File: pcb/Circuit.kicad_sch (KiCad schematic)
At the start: 46 parts, among them J1 DTM13-12PA-R008, J2 TSW-101-07-T-D, J3 TSW-101-07-T-D, U1 MCP1700-1802E_TO92, U2 CDP68HC68S1, U3 LM2672N-5.0, U4 Teensy4.0, U5 MCP2562-H-P

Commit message: CDP 3d model
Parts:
- removed D3: SD15_SOD323, Diode_THT:D_A-405_P7.62mm_Horizontal, symbol Diode:SD15_SOD323
- added D3: P6KE39CA, Diode_THT:D_DO-15_P10.16mm_Horizontal, symbol Diode_TVS_AKL:P6KE39CA
- C10: footprint Capacitor_THT:C_Radial_D5.0mm_H11.0mm_P2.00mm -> Capacitor_THT:C_Radial_D6.3mm_H7.0mm_P2.50mm
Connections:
- net +12V: now also D3.2 (A)
- net GND: now also D3.1 (K)

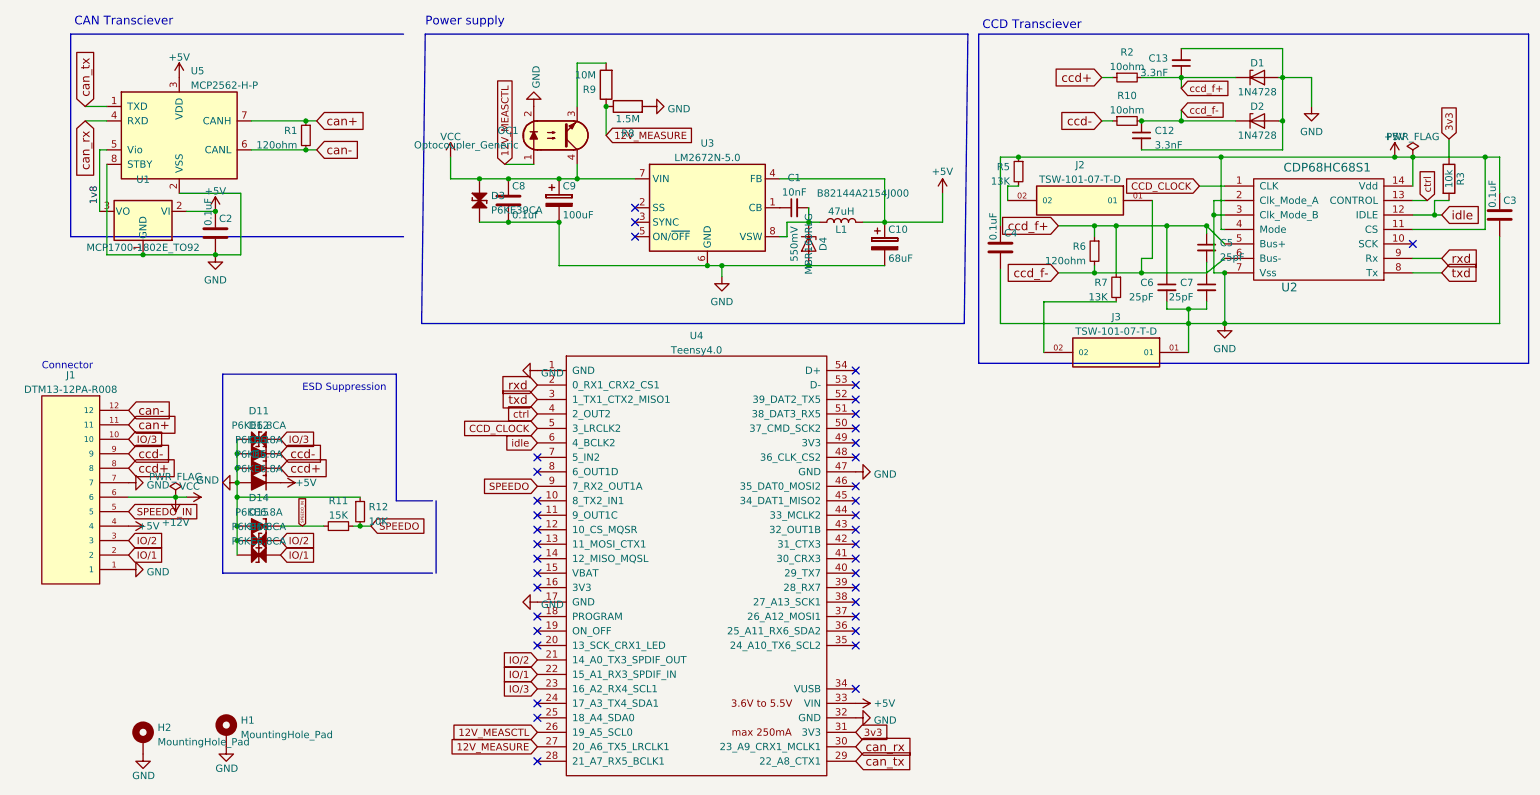
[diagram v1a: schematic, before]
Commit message: Add overvoltage protection to the 12v measure pin
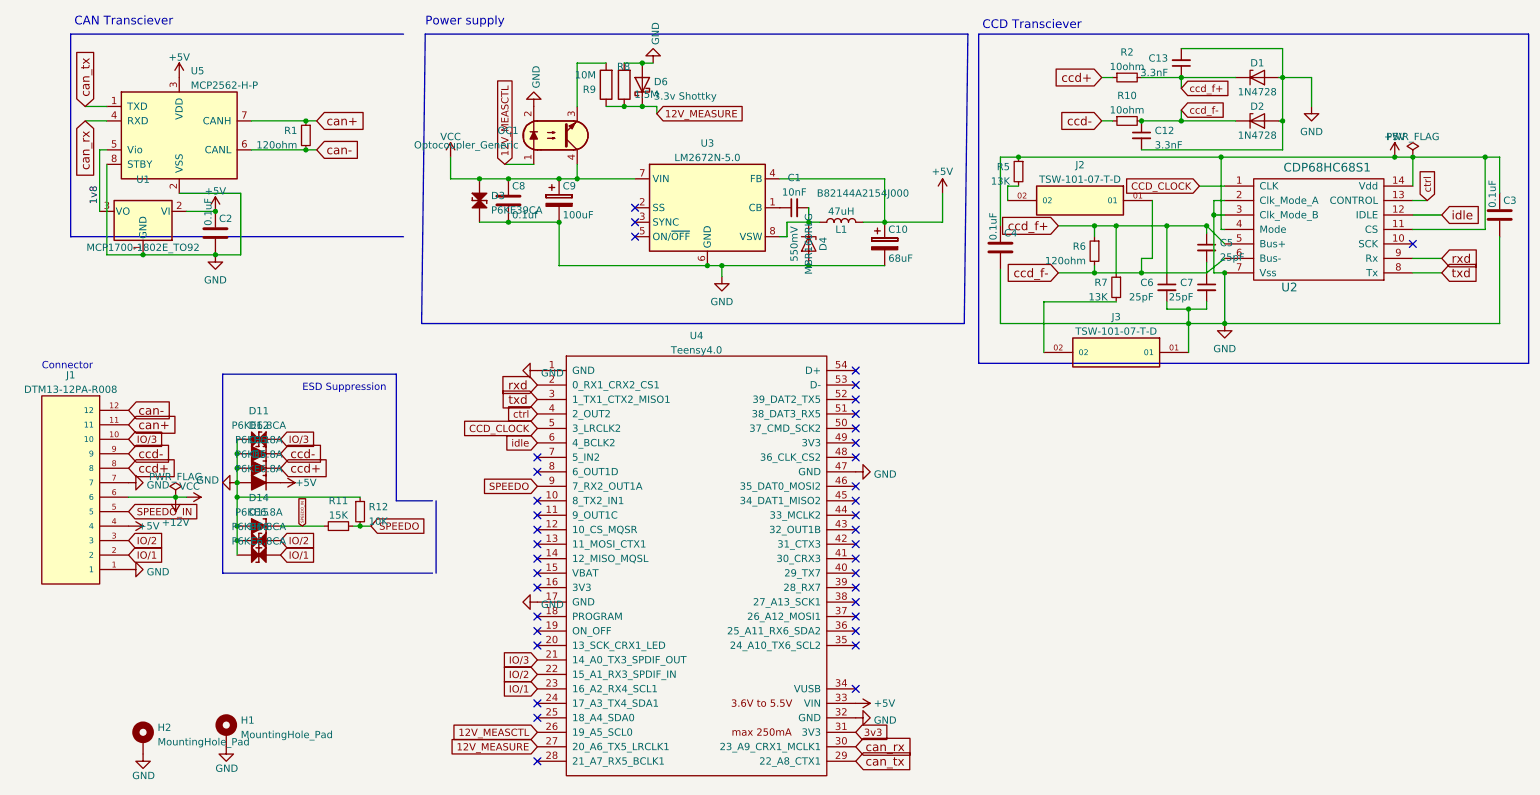
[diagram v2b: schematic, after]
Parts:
- removed R3: 10k, Resistor_THT:R_Axial_DIN0204_L3.6mm_D1.6mm_P5.08mm_Horizontal, symbol ccd_can_bridge-rescue:R
- added D6: 3.3v Shottky, Diode_THT:D_DO-34_SOD68_P7.62mm_Horizontal, symbol Device:D_Schottky
- C9: footprint Capacitor_THT:CP_Radial_D5.0mm_P2.50mm -> Capacitor_THT:CP_Radial_D8.0mm_P3.50mm
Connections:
- net 12V_MEASURE: now also D6.1 (K)
- net GND: now also D6.2 (A)
- net IO/1: now also U4.23 (16_A2_RX4_SCL1); no longer U4.22 (15_A1_RX3_SPDIF_IN)
- net IO/2: now also U4.22 (15_A1_RX3_SPDIF_IN); no longer U4.21 (14_A0_TX3_SPDIF_OUT)
- net IO/3: now also U4.21 (14_A0_TX3_SPDIF_OUT); no longer U4.23 (16_A2_RX4_SCL1)
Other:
- moved on the sheet: R8

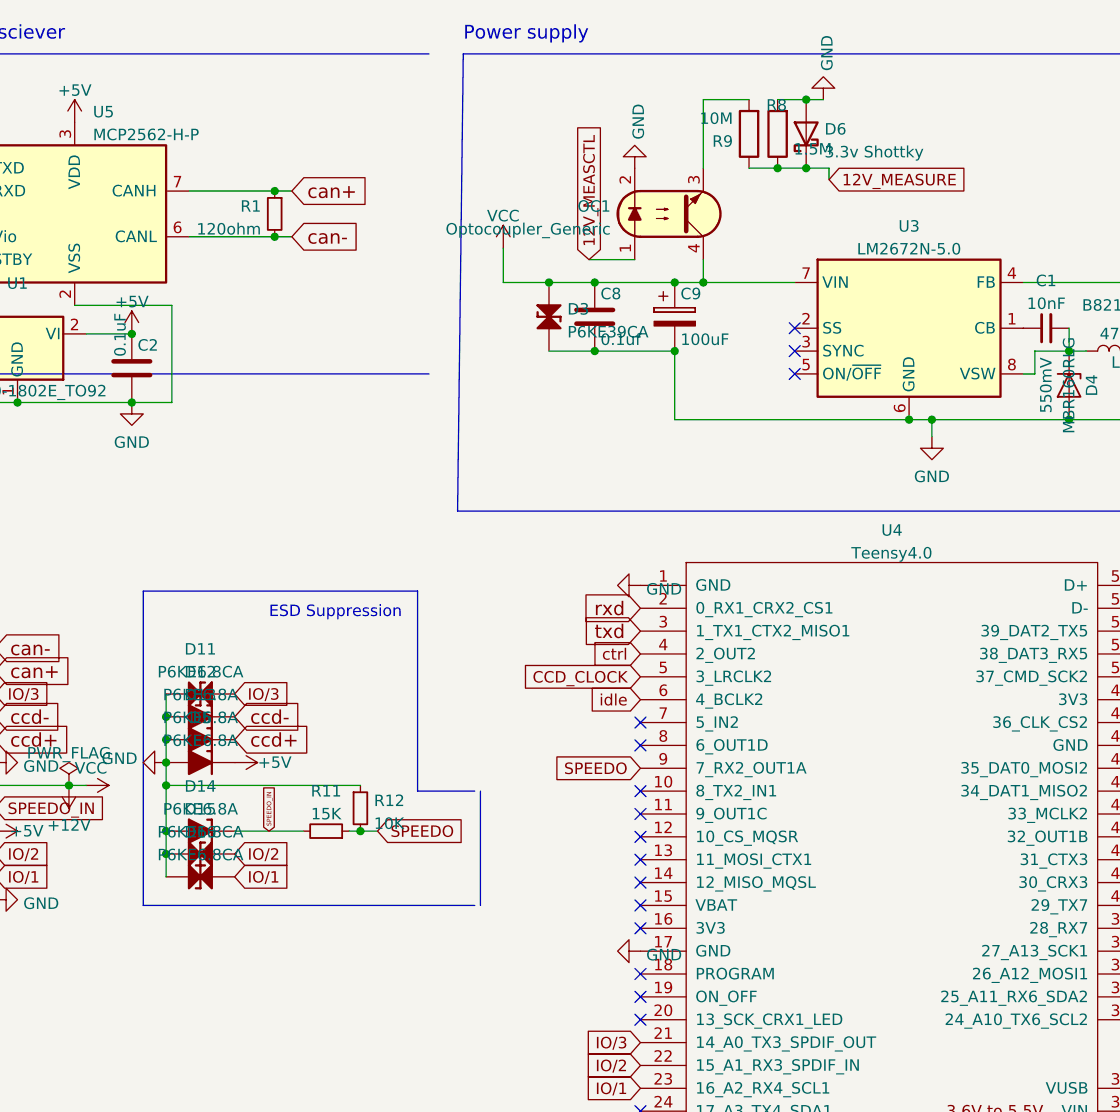
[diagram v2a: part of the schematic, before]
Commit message: Add 3.3v overvolt protection zeners
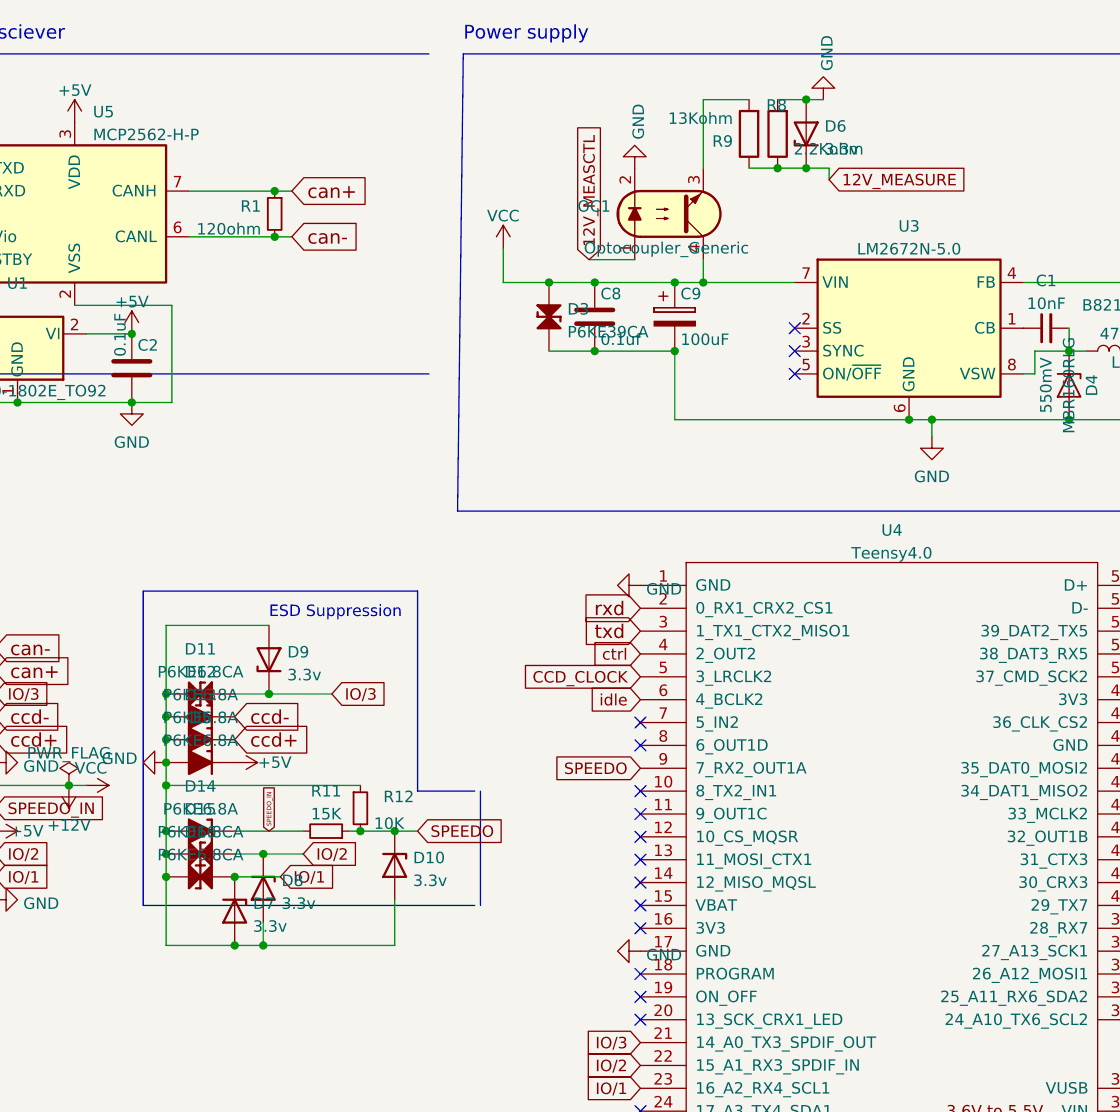
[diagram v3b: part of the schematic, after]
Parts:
- removed D6: 3.3v Shottky, Diode_THT:D_DO-34_SOD68_P7.62mm_Horizontal, symbol Device:D_Schottky
- added D10, D6, D7, D8, D9: 3.3v, Diode_THT:D_DO-35_SOD27_P7.62mm_Horizontal, symbol Device:D_Zener
- R8: value 1.5M -> 2.2Kohm
- R9: value 10M -> 13Kohm
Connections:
- net 12V_MEASURE: now also D6.1 (K)
- net GND: now also D10.2 (A), D6.2 (A), D7.2 (A), D8.2 (A), D9.2 (A)
- net IO/1: now also D7.1 (K)
- net IO/2: now also D8.1 (K)
- net IO/3: now also D9.1 (K)
- net SPEEDO: now also D10.1 (K)

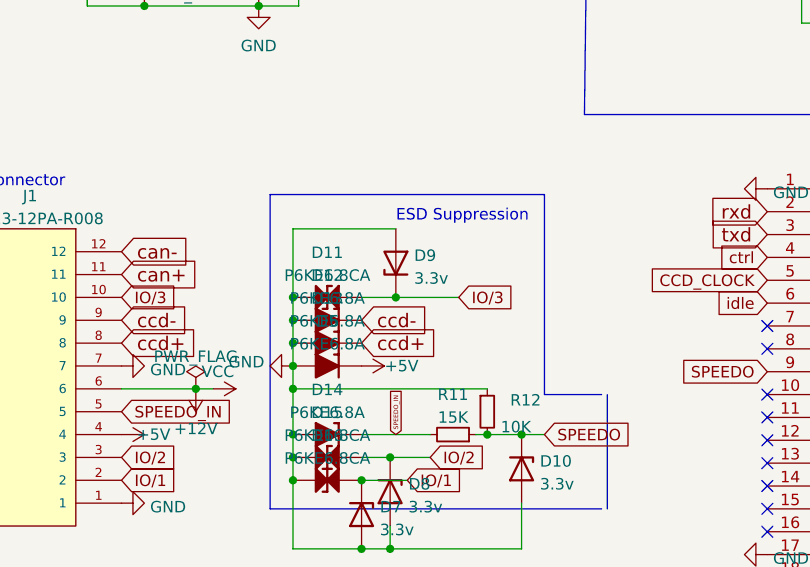
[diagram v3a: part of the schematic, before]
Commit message: Use correctly sized TVS diodes for the CCD bus
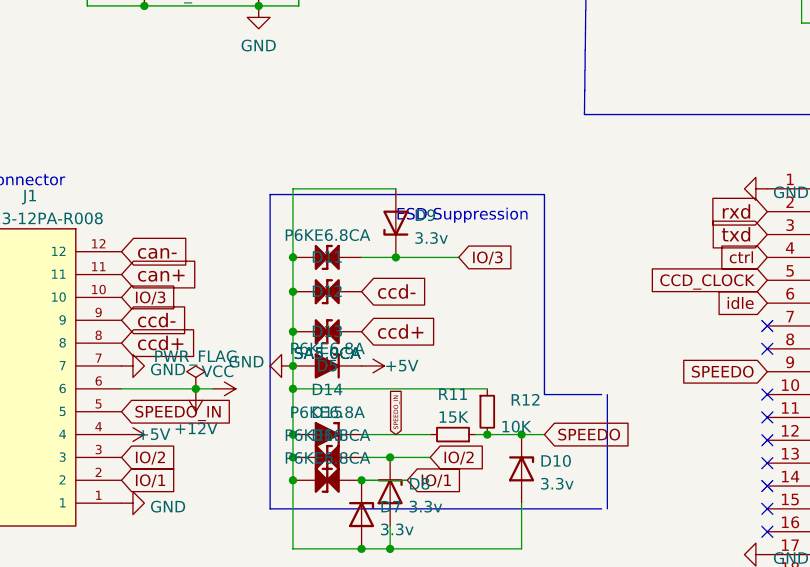
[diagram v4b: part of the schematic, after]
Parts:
- removed D12, D13: P6KE6.8A, Diode_THT:D_DO-15_P10.16mm_Horizontal, symbol Diode_TVS_AKL:P6KE6.8A
- added D12, D13: SA5.0CA, Diode_THT:D_DO-15_P10.16mm_Horizontal, symbol Diode_TVS_AKL:P6KE6.8CA
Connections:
- net GND: now also D12.2 (A), D13.2 (A)
- net ccd+: now also D13.1 (K)
- net ccd-: now also D12.1 (K)
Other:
- moved on the sheet: D11, D9
